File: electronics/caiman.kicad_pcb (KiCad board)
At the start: 2 copper layers, 90.9 x 93.9 mm, 134 parts, among them J1 Conn_01x03_Pin, J10 Conn_01x04_Pin, J11 Conn_01x04_Pin, J12 Conn_01x04_Pin, J13 Micro_SD_Card, J14 50 ohm, J15 Conn_01x03_Pin, J2 Conn_01x04_Pin, J3 Conn_01x04_Pin, J4 Conn_01x03_Pin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

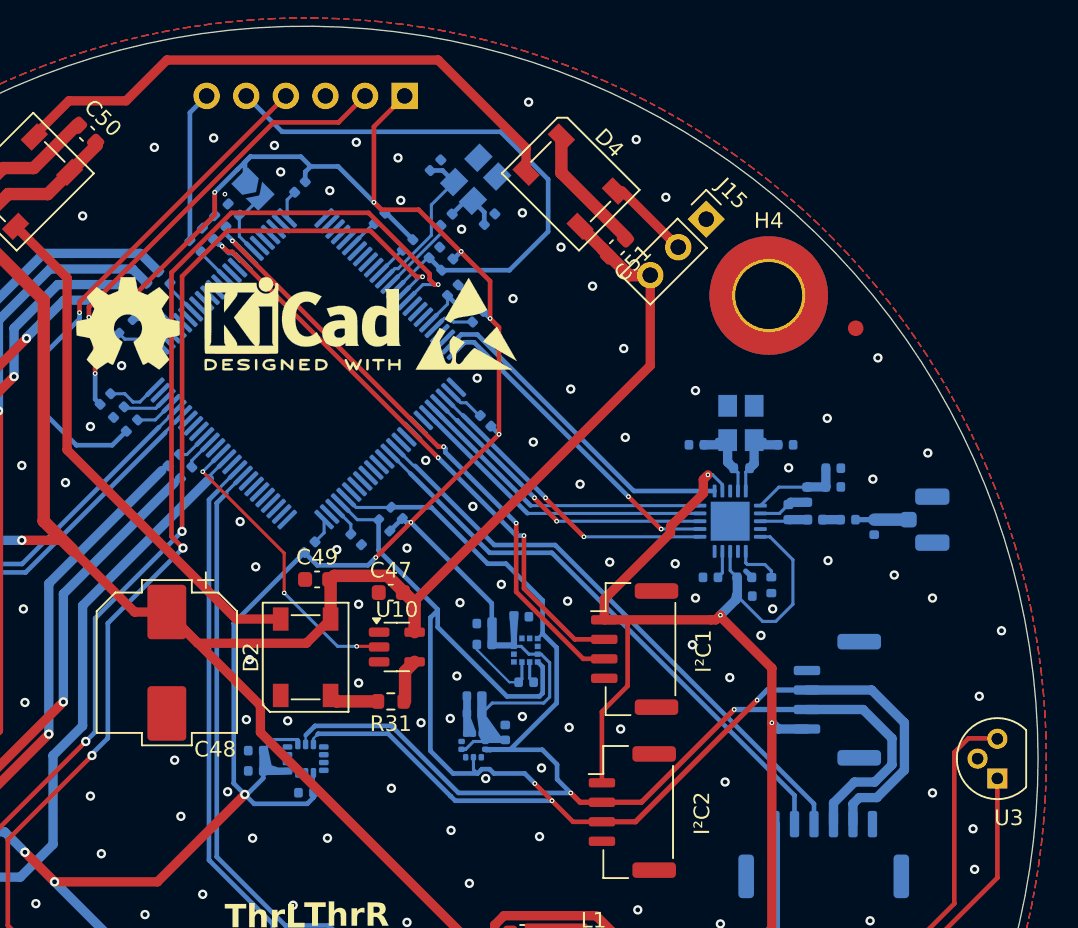
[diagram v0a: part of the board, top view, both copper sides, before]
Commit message: [Schm & PCB] Footprint correction
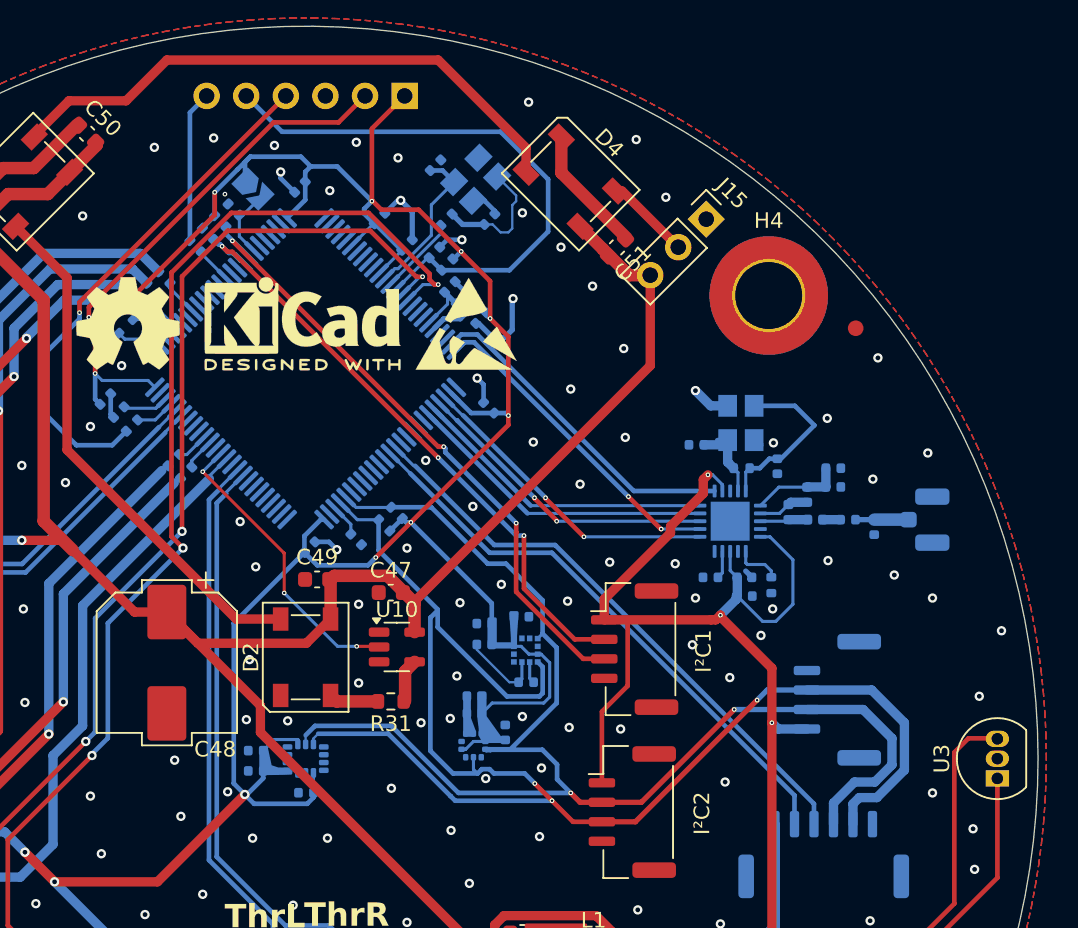
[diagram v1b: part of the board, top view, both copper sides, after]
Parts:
- U3: footprint Package_TO_SOT_THT:TO-92 -> Package_TO_SOT_THT:TO-92_Inline
- moved C39 1.47 mm to (180.2, 81.2), turned to -90 degrees
- moved C13 0.87 mm to (161.8, 77.5)
- moved C19 0.35 mm to (160.0, 70.5)
- moved C21 0.28 mm to (159.2, 69.8)
- moved C14 0.23 mm to (161.2, 71.8)
- turned C15 to -135 degrees
- turned C17 to -135 degrees
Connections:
- C12 pad 1: Net-(C12-Pad1) -> GND
- C13 pad 1: Net-(C13-Pad1) -> GND
- C14 pad 1: Net-(U7-VDDA) -> GND
- C15 pad 1: Net-(C15-Pad1) -> GND
- C16 pad 1: Net-(C16-Pad1) -> GND
- C17 pad 1: Net-(U7-VBAT) -> GND
- C18 pad 1: Net-(C18-Pad1) -> GND
- C28 pad 2: Net-(C28-Pad2) -> Net-(Y1-4)
- R13 pad 2: Net-(C28-Pad2) -> Net-(Y1-4)
- U7 pad 100: Net-(C16-Pad1) -> +3V3
- U7 pad 11: Net-(C15-Pad1) -> +3V3
- U7 pad 21: Net-(U7-VDDA) -> +3V3
- U7 pad 27: Net-(C13-Pad1) -> +3V3
- U7 pad 50: Net-(C12-Pad1) -> +3V3
- U7 pad 6: Net-(U7-VBAT) -> +3V3
- U7 pad 75: Net-(C18-Pad1) -> +3V3
- Y1 pad 3: GND -> Net-(Y1-4)
- Y1 pad 4: Net-(C28-Pad2) -> GND
- Y2 pad 3: GND -> Net-(U9-XC1)
- Y2 pad 4: Net-(U9-XC1) -> GND
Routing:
- net GND: track 22.3 -> 45.9 mm
- net +3V3: track 305.9 -> 328.6 mm
- net Net-(Y1-4): track 0.00 -> 8.38 mm
- net Net-(U9-XC1): track 5.81 -> 11.4 mm
- net Net-(C28-Pad2): track 3.50 -> 0.00 mm
- net Net-(C18-Pad1): track 3.44 -> 0.00 mm
- net Net-(U7-VDDA): track 2.81 -> 0.00 mm
- net Net-(C13-Pad1): track 2.45 -> 0.00 mm
- net Net-(C15-Pad1): track 2.09 -> 0.00 mm
- net Net-(U7-VBAT): track 1.92 -> 0.00 mm
- net Net-(C16-Pad1): track 1.85 -> 0.00 mm
- net Net-(C12-Pad1): track 1.67 -> 0.00 mm

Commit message: Finalization of PCB
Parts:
- moved R22 1.38 mm to (141.4, 82.6)
- moved C51 1.02 mm to (169.2, 66.5)
- moved J15 0.40 mm to (176.1, 65.4)
- moved C9 0.39 mm to (136.5, 119.2)
- moved D4 0.37 mm to (166.6, 62.9)
- moved C22 0.25 mm to (160.8, 95.8)
- moved C21 0.09 mm to (159.3, 69.8)
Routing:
- net Net-(U7-PC8): track 2.06 -> 3.50 mm
- net +3V3: track 328.6 -> 329.6 mm
- net /LED: track 19.1 -> 20.0 mm
- net /DAT0: track 30.9 -> 30.0 mm
- net +5V: track 190.4 -> 191.0 mm
- net GND: track 45.9 -> 45.4 mm
